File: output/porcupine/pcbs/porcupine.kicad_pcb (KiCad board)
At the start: 2 copper layers, 129.4 x 113.9 mm, 54 parts, among them J1 Jumper, J2 Jumper

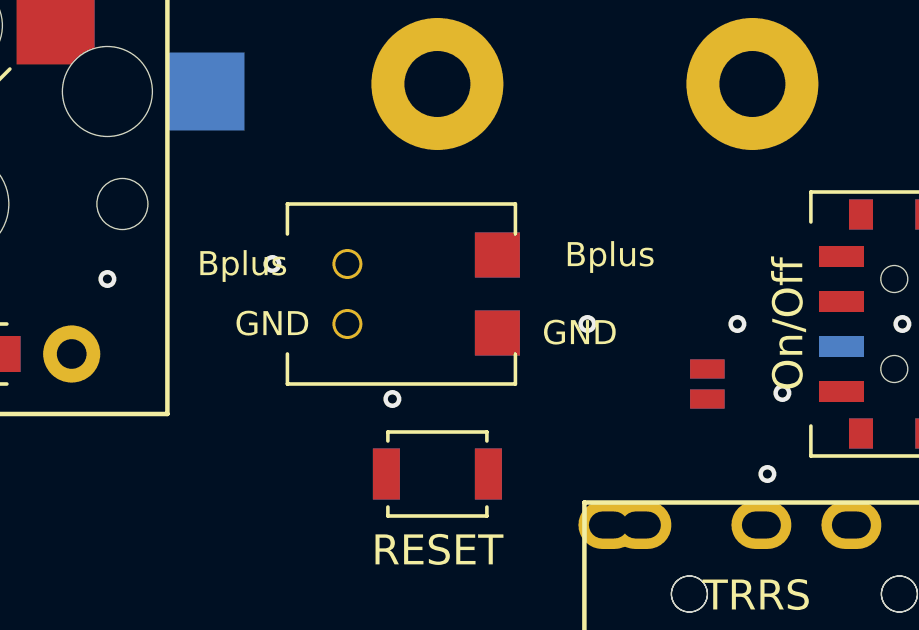
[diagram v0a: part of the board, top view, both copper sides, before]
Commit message: Update input and add manually routed boards
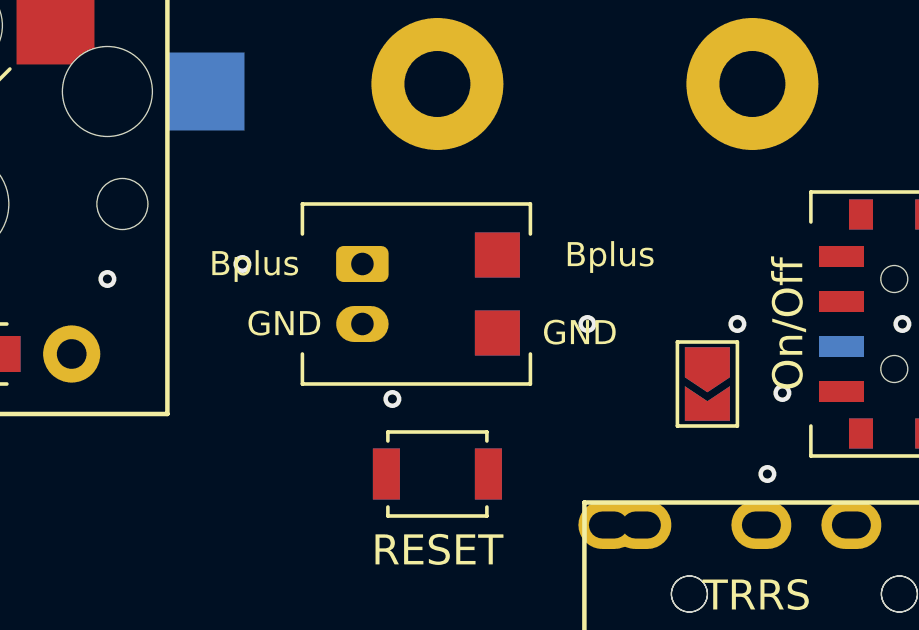
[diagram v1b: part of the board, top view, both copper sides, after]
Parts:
- D1, D10, D11, D12, D13, D14, D15, D16, D17, D18, D2, D3, D4, D5, D6, D7, D8, D9: footprint Diode_SMD:D_SOD-123 -> Diode_SMD:SOD-123
- J1: footprint PCM12SMTR -> Jumper:SolderJumper-2_P1.3mm_Open_TrianglePad1.0x1.5mm; moved to B.Cu
- J2: footprint PCM12SMTR -> Jumper:SolderJumper-2_P1.3mm_Open_TrianglePad1.0x1.5mm
- moved _2 0.50 mm to (259.9, 129.7)

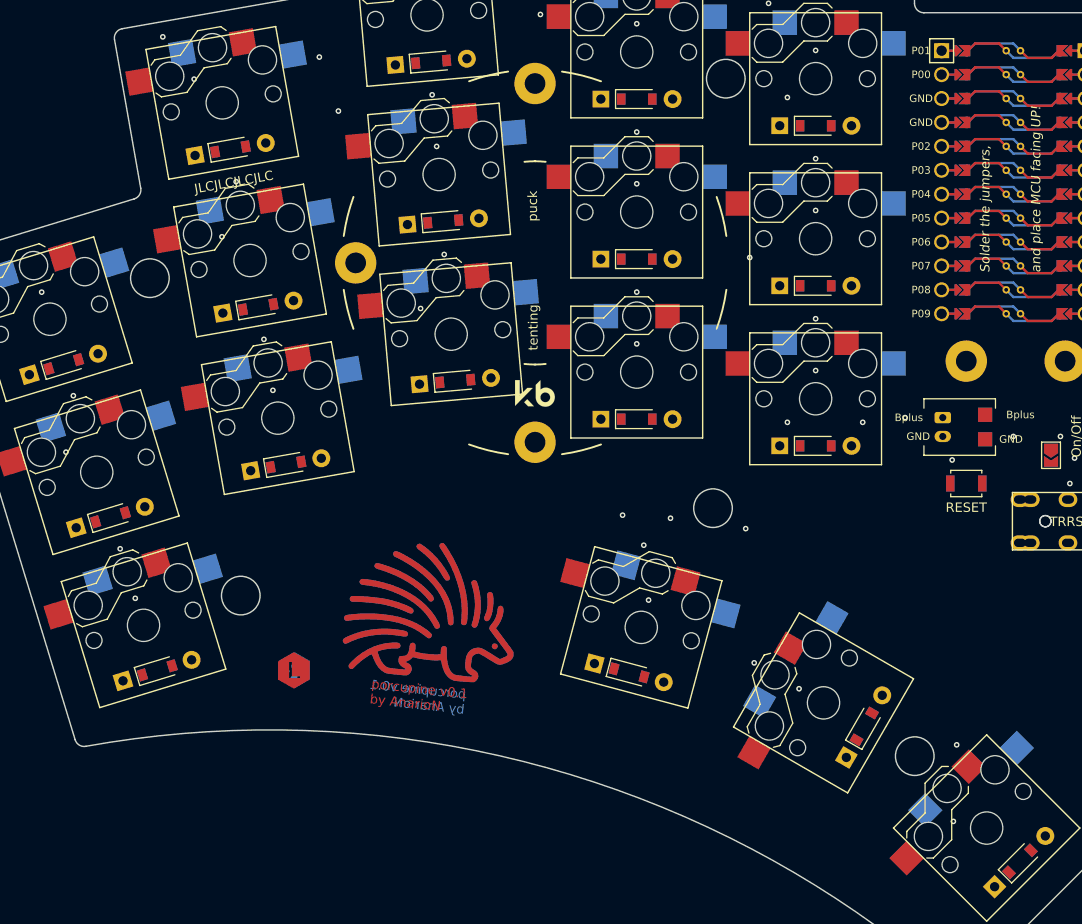
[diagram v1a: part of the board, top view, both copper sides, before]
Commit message: Add new logo
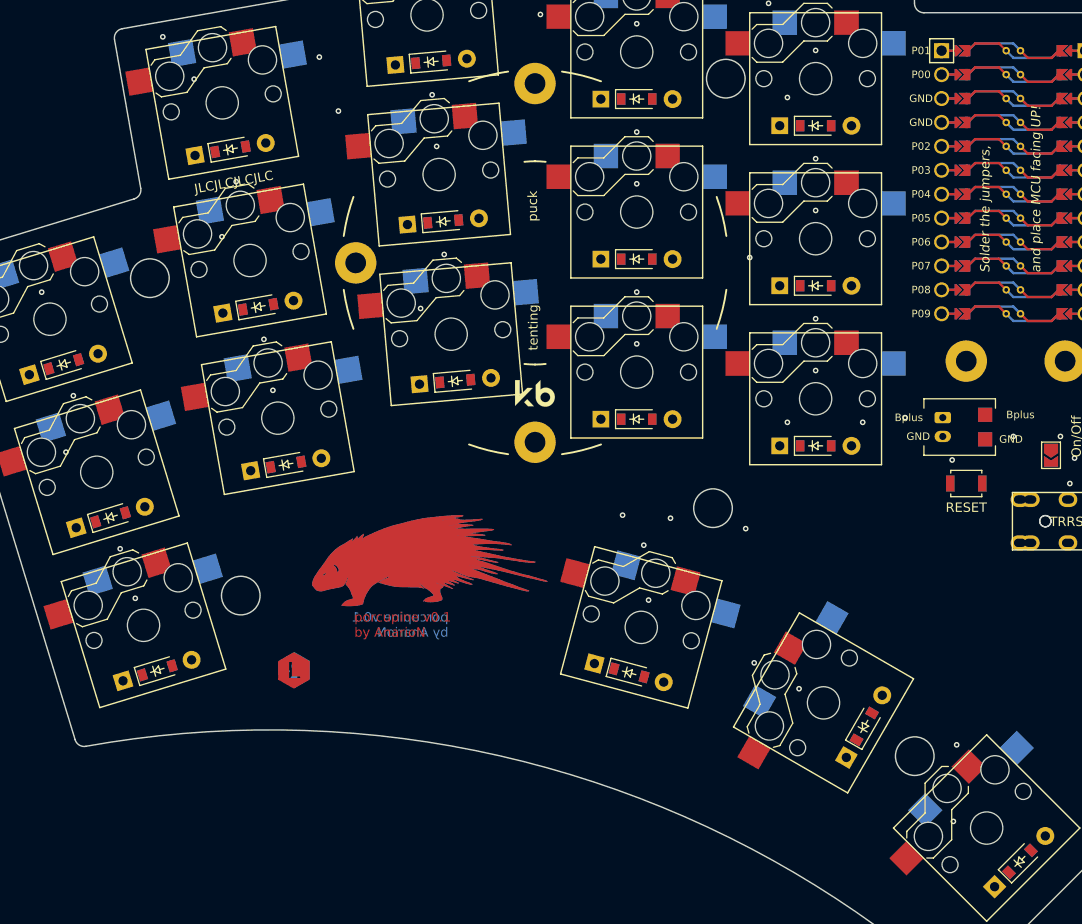
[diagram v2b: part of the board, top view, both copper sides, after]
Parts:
- moved LOGO_B 5.28 mm to (205.4, 143.9), turned to 0 degrees
- moved LOGO_F 5.28 mm to (205.4, 143.9), turned to 0 degrees

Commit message: 🔥 Remove old versions
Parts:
- removed LOGO_B, LOGO_F: , Porcupine Logo
- removed _9: Tenting Puck, Tenting Puck
- added D19: D_SOD-123, Diode_SMD:SOD-123, F.Cu at (228.1, 174.8)
- added D20: D_SOD-123, Diode_SMD:SOD-123, F.Cu at (246.9, 176.8)
- added D21: D_SOD-123, Diode_SMD:SOD-123, F.Cu at (271.7, 178.0)
- added D22: D_SOD-123, Diode_SMD:SOD-123, F.Cu at (289.8, 185.5)
- added D23: D_SOD-123, Diode_SMD:SOD-123, F.Cu at (273.5, 160.6)
- added Nice!View1: , lib:niceview_headers, F.Cu at (272.5, 134.6)
- added REF**: RollerEncoder_Panasonic_EVQWGD001, RollerEncoder_Panasonic_EVQWGD001, F.Cu at (272.5, 150.6)
- added S19: , PG1350, F.Cu at (228.3, 169.8)
- added S20: , PG1350, F.Cu at (247.6, 171.8)
- added S21: , PG1350, F.Cu at (266.9, 176.5)
- added S22: , PG1350, F.Cu at (285.2, 183.5)
- added _67: hole, Through Hole, F.Cu at (263.0, 138.6)
- added _68: hole, Through Hole, F.Cu at (282.0, 138.6)
- added _69: hole, Through Hole, F.Cu at (162.6, 124.5)
- added _7: Tenting Puck, Tenting Puck, F.Cu at (221.0, 133.6)
- added _70: hole, Through Hole, F.Cu at (162.6, 141.5)
- added _71: hole, Through Hole, F.Cu at (182.9, 117.7)
- added _72: hole, Through Hole, F.Cu at (182.9, 151.7)
- added _75: hole, Through Hole, F.Cu at (254.0, 183.0)
- moved S18 59.6 mm to (249.5, 114.6), turned to 0 degrees
- moved D18 59.2 mm to (249.5, 119.6), turned to 0 degrees
- moved _3 56.2 mm to (230.5, 99.7), turned to 180 degrees
- moved _74 49.6 mm to (238.6, 158.5)
- moved J1 46.0 mm to (238.5, 100.6), turned to 90 degrees
- moved J2 46.0 mm to (238.5, 100.6), turned to 90 degrees
- moved TRRS_B 43.0 mm to (288.3, 97.6), turned to 0 degrees
- moved TRRS_F 43.0 mm to (288.3, 97.6), turned to 0 degrees
- moved PAD2 33.9 mm to (250.5, 100.1)
- moved _4_B 33.6 mm to (288.5, 114.6)
- moved _4_F 33.6 mm to (288.5, 114.6)
- moved _2 31.4 mm to (247.0, 101.1)
- moved D7 30.3 mm to (192.5, 150.8), turned to 0 degrees
- moved S7 30.1 mm to (192.5, 145.8), turned to 0 degrees
- moved PAD1 29.8 mm to (250.5, 102.1)
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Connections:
- net P0 renamed trrs
- D1 pad 1: pinky_bottom -> outer_bottom
- D1 pad 2: P6 -> outer_bottom
- D10 pad 1: index_bottom -> middle_bottom
- D10 pad 2: P6 -> middle_bottom
- D11 pad 1: index_home -> middle_home
- D11 pad 2: P5 -> middle_home
- D12 pad 1: index_top -> middle_top
- D12 pad 2: P4 -> middle_top
- D13 pad 1: inner_bottom -> index_bottom
- D13 pad 2: P6 -> index_bottom
- D14 pad 1: inner_home -> index_home
- D14 pad 2: P5 -> index_home
- D15 pad 1: inner_top -> index_top
- D15 pad 2: P4 -> index_top
- D16 pad 1: near_thumb -> inner_bottom
- D16 pad 2: P7 -> inner_bottom
- D17 pad 1: home_thumb -> inner_home
- D17 pad 2: P7 -> inner_home
- D18 pad 1: far_thumb -> inner_top
- D18 pad 2: P7 -> inner_top
- D2 pad 1: pinky_home -> outer_home
- D2 pad 2: P5 -> outer_home
- D3 pad 1: pinky_top -> outer_top
- D3 pad 2: P4 -> outer_top
- D4 pad 1: ring_bottom -> pinky_bottom
- D4 pad 2: P6 -> pinky_bottom
- D5 pad 1: ring_home -> pinky_home
- D5 pad 2: P5 -> pinky_home
- D6 pad 1: ring_top -> pinky_top
- D6 pad 2: P4 -> pinky_top
- D7 pad 1: middle_bottom -> ring_bottom
- D7 pad 2: P6 -> ring_bottom
- D8 pad 1: middle_home -> ring_home
- D8 pad 2: P5 -> ring_home
- D9 pad 1: middle_top -> ring_top
- D9 pad 2: P4 -> ring_top
- MCU1 pad 10: P14 -> col_middle
- MCU1 pad 11: P16 -> col_index
- MCU1 pad 12: P10 -> col_inner
- MCU1 pad 15: P7 -> row_thumb
- MCU1 pad 16: P6 -> row_bottom
- MCU1 pad 17: P5 -> row_home
- MCU1 pad 18: P4 -> row_top
- MCU1 pad 19: P3 -> SCL
- MCU1 pad 20: P2 -> SDA
- MCU1 pad 24: P1 -> CS
- MCU1 pad 5: P21 -> ENCB
- MCU1 pad 6: P20 -> ENCA
- MCU1 pad 7: P19 -> col_outer
- MCU1 pad 8: P18 -> col_pinky
- MCU1 pad 9: P15 -> col_ring
- S1 pad 1: pinky_bottom -> outer_bottom
- S1 pad 2: P20 -> col_outer
- S10 pad 1: index_bottom -> middle_bottom
- S10 pad 2: P15 -> col_middle
- S11 pad 1: index_home -> middle_home
- S11 pad 2: P15 -> col_middle
- S12 pad 1: index_top -> middle_top
- S12 pad 2: P15 -> col_middle
- S13 pad 1: inner_bottom -> index_bottom
- S13 pad 2: P14 -> col_index
- S14 pad 1: inner_home -> index_home
- S14 pad 2: P14 -> col_index
- S15 pad 1: inner_top -> index_top
- S15 pad 2: P14 -> col_index
- S16 pad 1: near_thumb -> inner_bottom
- S16 pad 2: P18 -> col_inner
- S17 pad 1: home_thumb -> inner_home
- S17 pad 2: P15 -> col_inner
- S18 pad 1: far_thumb -> inner_top
- S18 pad 2: P14 -> col_inner
- S2 pad 1: pinky_home -> outer_home
- S2 pad 2: P20 -> col_outer
- S3 pad 1: pinky_top -> outer_top
- S3 pad 2: P20 -> col_outer
- S4 pad 1: ring_bottom -> pinky_bottom
- S4 pad 2: P19 -> col_pinky
- S5 pad 1: ring_home -> pinky_home
- S5 pad 2: P19 -> col_pinky
- S6 pad 1: ring_top -> pinky_top
- S6 pad 2: P19 -> col_pinky
- S7 pad 1: middle_bottom -> ring_bottom
- S7 pad 2: P18 -> col_ring
- S8 pad 1: middle_home -> ring_home
- S8 pad 2: P18 -> col_ring
- S9 pad 1: middle_top -> ring_top
- S9 pad 2: P18 -> col_ring
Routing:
- net outer_top: vias 0 -> 1
- net outer_home: vias 0 -> 1
- net outer_bottom: vias 0 -> 1
- net inner_thumb: vias 0 -> 1
- net col_ring: vias 0 -> 4
- net col_pinky: vias 0 -> 3
- net col_outer: vias 0 -> 3
- net col_middle: vias 0 -> 4
- net col_inner: vias 0 -> 4
- net col_index: vias 0 -> 4
- net RST: vias 2 -> 0
- net RAW: vias 1 -> 0
- net P20: vias 3 -> 0
- net P19: vias 3 -> 0
- net P18: vias 5 -> 0
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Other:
- board size 129.4 x 113.9 mm -> 165.2 x 103.2 mm
- net class Default removed
- net class Power removed
- board text added: "porcupine v2.0 by AnarioN"
- board text removed: "porcupine v0.1 by AnarioN"
